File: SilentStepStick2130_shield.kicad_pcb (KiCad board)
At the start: 4 copper layers, 68.6 x 53.3 mm, 15 parts, among them J1 Conn_01x03, U1 TMC2130_SILENTSTEPSTICK, U2 TMC2130_SILENTSTEPSTICK

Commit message: v0
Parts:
- added J2: Conn_01x04_Socket, LibPersoNadj:CUI_TBL009-254-04BK-2OR, F.Cu at (163.2, 87.7)
- added J5: Conn_01x03, Connector_PinHeader_2.54mm:PinHeader_1x03_P2.54mm_Vertical, F.Cu at (128.9, 73.7)
- J1: value Conn_01x03 -> Conn_01x04_Socket; footprint Connector_PinHeader_2.54mm:PinHeader_1x03_P2.54mm_Vertical -> LibPersoNadj:CUI_TBL009-254-04BK-2OR
- moved J1 30.1 mm to (163.2, 61.6), turned to 90 degrees
- moved U1 23.8 mm to (143.5, 64.6)
- moved U2 23.8 mm to (143.5, 86.8)
- moved C1 20.3 mm to (156.2, 95.6), turned to 0 degrees
- moved C2 20.1 mm to (156.2, 73.5), turned to 0 degrees
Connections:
- C1 pad 1: +5V -> /VM
- C2 pad 1: +5V -> /VM
- IOL1 pad 5: /DIR_2 -> /IO4
- IOL1 pad 6: /DIR_1 -> /IO5
- IOL1 pad 7: /IO6 -> /DIR_2
- IOL1 pad 8: /IO7 -> /DIR_1
- J1 pad 1: +5V -> /OA2_1
- J1 pad 2: +5V -> /OA1_1
- J1 pad 3: /VIN -> /OB1_1
- U1 pad 2: /IO3 -> /IO5
- U1 pad 8: /IO7 -> /IO3
- U1 pad 9: +5V -> /VM
- U2 pad 2: /IO2 -> /IO4
- U2 pad 8: /IO6 -> /IO2
- U2 pad 9: +5V -> /VM
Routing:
- net /IO2: track 0.00 -> 72.3 mm
- net /CS_2: track 0.00 -> 55.4 mm
- net /IOREF: track 0.00 -> 55.0 mm
- net /VM: track 0.00 -> 52.1 mm
- net /SCK: track 0.00 -> 50.9 mm
- net /IO4: track 0.00 -> 48.6 mm
- net /MOSI: track 0.00 -> 47.2 mm
- net +5V: track 0.00 -> 45.9 mm
- net /MISO: track 0.00 -> 42.0 mm
- net /IO3: track 0.00 -> 40.5 mm
- net /VIN: track 0.00 -> 40.2 mm
- net /DIR_2: track 0.00 -> 39.3 mm
- net /CS_1: track 0.00 -> 28.5 mm
- net /IO5: track 0.00 -> 25.8 mm
- net /OB1_1: track 0.00 -> 21.2 mm
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
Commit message: v0 sent to fab
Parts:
- moved J5 39.5 mm to (162.6, 94.3), turned to 90 degrees
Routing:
- net +5V: track 45.9 -> 20.4 mm
- net /VIN: track 40.2 -> 17.0 mm
- net /VM: track 52.1 -> 49.0 mm
- net /CS_2: track 55.4 -> 53.3 mm
- net /SCK: track 50.9 -> 51.4 mm
- net GND: vias 368 -> 646

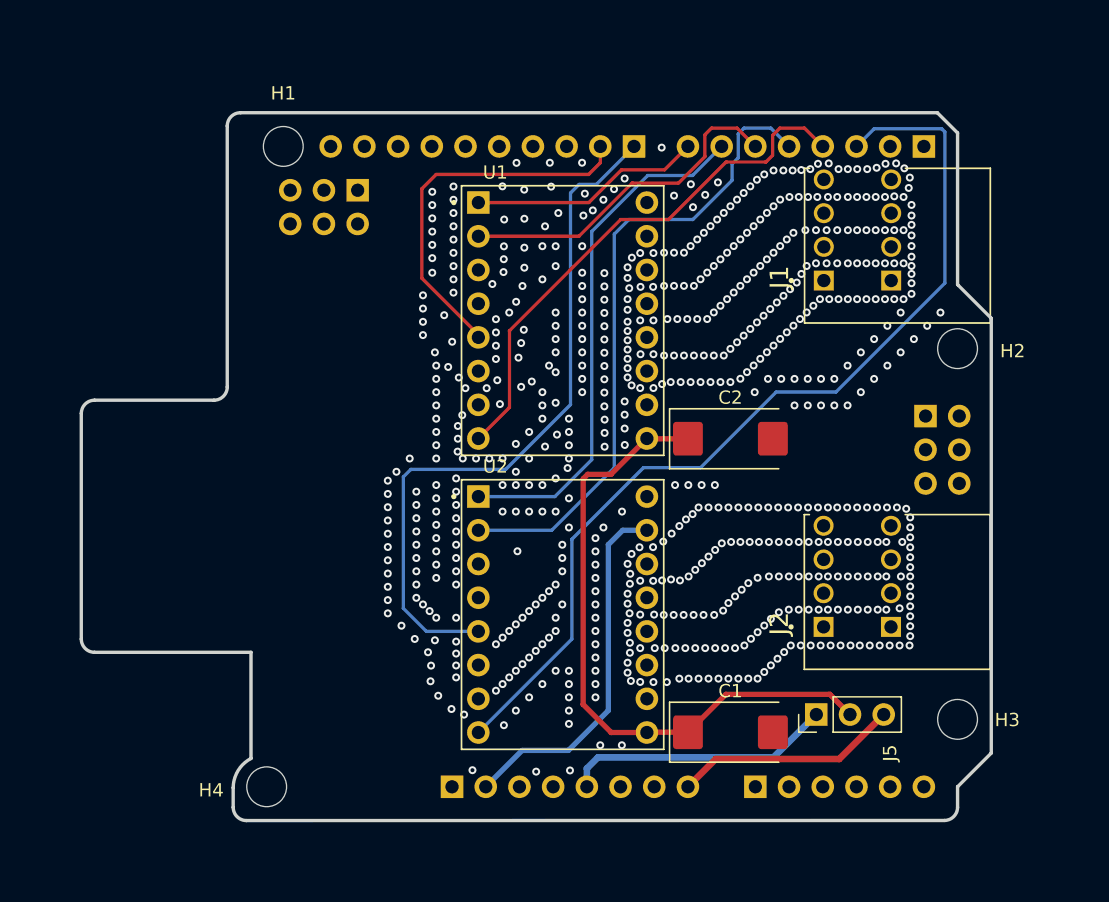
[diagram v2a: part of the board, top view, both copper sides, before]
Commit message: Changed to the new arduino symbol and moved the chipSelect from 11 12 to 12 13 Hard set enables to GND to get 3 digital input free for endcourse contacts Fliped the TMC2130 so that their backside faced up (changed the footprint)
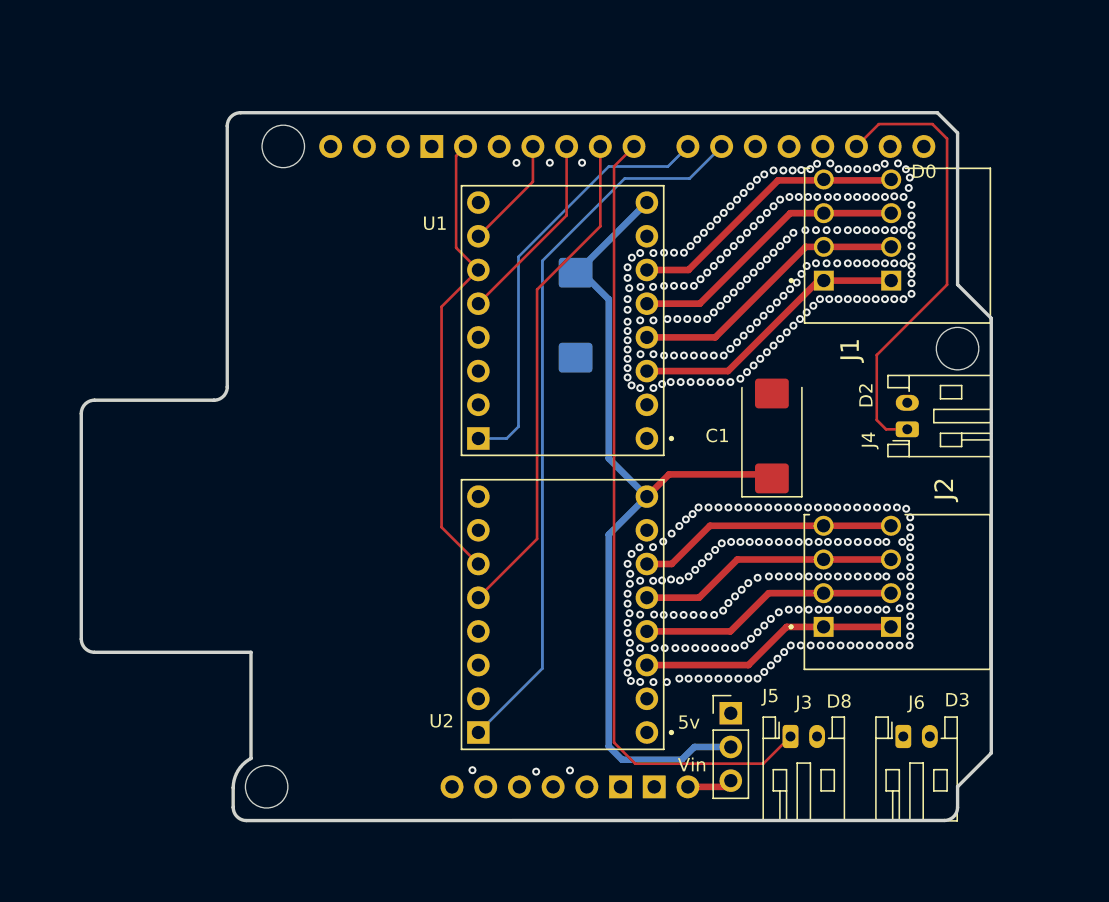
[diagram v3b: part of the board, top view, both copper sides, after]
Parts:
- removed AD1: Conn_01x06_Socket, Connector_PinHeader_2.54mm:PinHeader_1x06_P2.54mm_Vertical
- removed H1, H2, H3, H4: MountingHole, MountingHole:MountingHole_3mm
- removed ICSP1, ICSP2: Conn_02x03_Odd_Even, Connector_PinSocket_2.54mm:PinSocket_2x03_P2.54mm_Vertical
- removed IOH1: Conn_01x10_Socket, Connector_PinHeader_2.54mm:PinHeader_1x10_P2.54mm_Vertical
- removed IOL1, POWER1: Conn_01x08_Socket, Connector_PinHeader_2.54mm:PinHeader_1x08_P2.54mm_Vertical
- added A1: Arduino_Uno_R3_Shield, LibPersoNadj:Arduino_Uno_R3_Shield, F.Cu at (141.5, 75.6)
- added J3: Conn_01x02_Pin, Connector_JST:JST_PH_S2B-PH-K_1x02_P2.00mm_Horizontal, F.Cu at (160.7, 96.0)
- added J4: Conn_01x02_Pin, Connector_JST:JST_PH_S2B-PH-K_1x02_P2.00mm_Horizontal, F.Cu at (169.5, 72.8)
- added J6: Conn_01x02_Pin, Connector_JST:JST_PH_S2B-PH-K_1x02_P2.00mm_Horizontal, F.Cu at (169.2, 96.0)
- C2: moved to B.Cu
- moved C1 22.5 mm to (159.3, 73.3), turned to 90 degrees
- moved C2 14.9 mm to (144.5, 64.2), turned to -90 degrees
- moved J5 6.45 mm to (156.2, 94.2), turned to 0 degrees
- turned U1 to 180 degrees
- turned U2 to 180 degrees
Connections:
- J1 pad 1: /OA2_1 -> /OB2_1
- J1 pad 2: /OA1_1 -> /OB1_1
- J1 pad 3: /OB1_1 -> /OA1_1
- J1 pad 4: /OB2_1 -> /OA2_1
- J2 pad 1: /OA2_2 -> /OB2_2
- J2 pad 2: /OA1_2 -> /OB1_2
- J2 pad 3: /OB1_2 -> /OA1_2
- J2 pad 4: /OB2_2 -> /OA2_2
- U1 pad 2: /IO5 -> /STEP_1
- U1 pad 8: /IO3 -> GND
- U2 pad 2: /IO4 -> /STEP_2
- U2 pad 8: /IO2 -> GND
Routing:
- net Net-(A1-D3_INT1): track 0.00 -> 85.1 mm
- net /IO2: track 72.3 -> 0.00 mm
- net Net-(J3-Pin_1): track 0.00 -> 60.3 mm
- net /STEP_2: track 0.00 -> 57.4 mm
- net /IO4: track 48.6 -> 0.00 mm
- net /IO3: track 40.5 -> 0.00 mm
- net /STEP_1: track 0.00 -> 34.1 mm
- net Net-(A1-D2_INT0): track 0.00 -> 34.0 mm
- net /IO5: track 25.8 -> 0.00 mm
- net +5V: track 20.4 -> 0.00 mm
- net /VM: track 49.0 -> 67.2 mm
- net /SCK: track 51.4 -> 34.7 mm
- net /CS_2: track 53.3 -> 37.8 mm
- net /DIR_2: track 39.3 -> 54.6 mm
- net /MOSI: track 47.2 -> 32.1 mm
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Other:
- board text added: "5v Vin"
- board text added: "D2"
- board text added: "D3"
- board text added: "D8"

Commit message: v1
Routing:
- net Net-(A1-D3_INT1): track 85.1 -> 86.9 mm
- net /DIR_1: track 32.4 -> 33.2 mm
- net /MISO: track 40.0 -> 39.2 mm
- net /STEP_2: track 57.4 -> 56.8 mm
- net Net-(J3-Pin_1): track 60.3 -> 59.7 mm

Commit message: modified shield footprint to reconnect 5v and gnd.kicad_pcb
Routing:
- net +5V: track 0.00 -> 13.9 mm
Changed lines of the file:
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@@
 				(font
 					(size 1.27 1.27)
+					(thickness 0.15)
 				)
 			)
@@
 				(font
 					(size 1.27 1.27)
+					(thickness 0.15)
 				)
 			)
@@
 				(font
 					(size 1.27 1.27)
+					(thickness 0.15)
 				)
 			)
@@
 				(font
 					(size 1.27 1.27)
+					(thickness 0.15)
 				)
 			)
@@
 				(font
 					(size 1.27 1.27)
+					(thickness 0.15)
 				)
 			)
@@
 				(font
 					(size 1.27 1.27)
+					(thickness 0.15)
 				)
 			)
@@
 				(font
 					(size 1.27 1.27)
+					(thickness 0.15)
 				)
 			)
@@
 				(font
 					(size 1.27 1.27)
+					(thickness 0.15)
 				)
 			)
@@
 				(font
 					(size 1.27 1.27)
+					(thickness 0.15)
 				)
 			)
@@
 				(font
 					(size 1.27 1.27)
+					(thickness 0.15)
 				)
 			)
@@
 				(font
 					(size 1.27 1.27)
+					(thickness 0.15)
 				)
 			)
@@
 				(font
 					(size 1.27 1.27)
+					(thickness 0.15)
 				)
 			)
@@
 				(font
 					(size 1.27 1.27)
+					(thickness 0.15)
 				)
 			)
@@
 				(font
 					(size 1.27 1.27)
+					(thickness 0.15)
 				)
 			)
@@
 				(font
 					(size 1.27 1.27)
+					(thickness 0.15)
 				)
 			)
@@
 				(font
 					(size 1.27 1.27)
+					(thickness 0.15)
 				)
 			)
@@
 				(font
 					(size 1.27 1.27)
+					(thickness 0.15)
 				)
 			)
@@
 				(font
 					(size 1.27 1.27)
+					(thickness 0.15)
 				)
 			)
@@
 				(font
 					(size 1.27 1.27)
+					(thickness 0.15)
 				)
 			)
@@
 				(font
 					(size 1.27 1.27)
+					(thickness 0.15)
 				)
 			)
@@
 				(font
 					(size 1.27 1.27)
+					(thickness 0.15)
 				)
 			)
@@
 				(font
 					(size 1.27 1.27)
+					(thickness 0.15)
 				)
 			)
@@
 				(font
 					(size 1.27 1.27)
+					(thickness 0.15)
 				)
 			)
@@
 				(font
 					(size 1.27 1.27)
+					(thickness 0.15)
 				)
 			)
@@
 			(pintype "power_out+no_connect")
 		)
-		(pad "5V" thru_hole oval
+		(pad "5V1" thru_hole oval
 			(at 3.81 24.13)
 			(size 1.7272 1.7272)
@@
 			(layers "*.Cu" "*.Mask")
 			(remove_unused_layers no)
+			(net 8 "+5V")
+			(pinfunction "5V")
+			(pintype "power_in")
 		)
 		(pad "AREF" thru_hole oval
@@
 			(pintype "bidirectional")
 		)
-		(pad "GND" thru_hole rect
-			(at -7.874 -24.13)
+		(pad "GND1" thru_hole rect
+			(at 6.35 24.13)
 			(size 1.7272 1.7272)
 			(drill 1.016)
 			(layers "*.Cu" "*.Mask")
 			(remove_unused_layers no)
+			(net 6 "GND")
+			(pinfunction "GND")
+			(pintype "power_in")
 		)
-		(pad "GND" thru_hole rect
-			(at 6.35 24.13)
+		(pad "GND2" thru_hole rect
+			(at 8.89 24.13)
 			(size 1.7272 1.7272)
 			(drill 1.016)
 			(layers "*.Cu" "*.Mask")
 			(remove_unused_layers no)
+			(net 6 "GND")
+			(pinfunction "GND")
+			(pintype "power_in")
 		)
-		(pad "GND" thru_hole rect
-			(at 8.89 24.13)
+		(pad "GND3" thru_hole rect
+			(at -7.874 -24.13)
 			(size 1.7272 1.7272)
 			(drill 1.016)
 			(layers "*.Cu" "*.Mask")
 			(remove_unused_layers no)
+			(net 6 "GND")
+			(pinfunction "GND")
+			(pintype "power_in")
 		)
 		(pad "IORF" thru_hole oval
@@
 		)
 		(model "${KICAD8_3DMODEL_DIR}/Connector_PinHeader_2.54mm.3dshapes/PinHeader_1x06_P2.54mm_Vertical.step"
-			(hide yes)
 			(offset
 				(xyz 16.5 -24.1 -1.7)
@@
 		)
 		(model "${KICAD8_3DMODEL_DIR}/Connector_PinSocket_2.54mm.3dshapes/PinSocket_2x03_P2.54mm_Vertical.step"
-			(hide yes)
 			(offset
 				(xyz 29.337 3.81 -1.7)
@@
 				(font
 					(size 1.27 1.27)
+					(thickness 0.15)
 				)
 			)
@@
 				(font
 					(size 1.27 1.27)
+					(thickness 0.15)
 				)
 			)
@@
 				(font
 					(size 1.27 1.27)
+					(thickness 0.15)
 				)
 			)
@@
 				(font
 					(size 1.27 1.27)
+					(thickness 0.15)
 				)
 			)
@@
 				(font
 					(size 1.27 1.27)
+					(thickness 0.15)
 				)
 			)
@@
 				(font
 					(size 1.27 1.27)
+					(thickness 0.15)
 				)
 			)
@@
 				(font
 					(size 1.27 1.27)
+					(thickness 0.15)
 				)
 				(justify mirror)
@@
 				(font
 					(size 1.27 1.27)
+					(thickness 0.15)
 				)
 				(justify mirror)
@@
 				(font
 					(size 1.27 1.27)
+					(thickness 0.15)
 				)
 				(justify mirror)
@@
 	)
 	(segment
+		(start 145.35 99.746223)
+		(end 145.35 98.5)
+		(width 0.4)
+		(layer "In2.Cu")
+		(net 8)
+	)
+	(segment
+		(start 151.81 97.54)
+		(end 155.15 94.2)
+		(width 0.4)
+		(layer "In2.Cu")
+		(net 8)
+	)
+	(segment
+		(start 146.31 97.54)
+		(end 151.81 97.54)
+		(width 0.4)
+		(layer "In2.Cu")
+		(net 8)
+	)
+	(segment
+		(start 145.35 98.5)
+		(end 146.31 97.54)
+		(width 0.4)
+		(layer "In2.Cu")
+		(net 8)
+	)
+	(segment
+		(start 155.15 94.2)
+		(end 156.2 94.2)
+		(width 0.4)
+		(layer "In2.Cu")
+		(net 8)
+	)
+	(segment

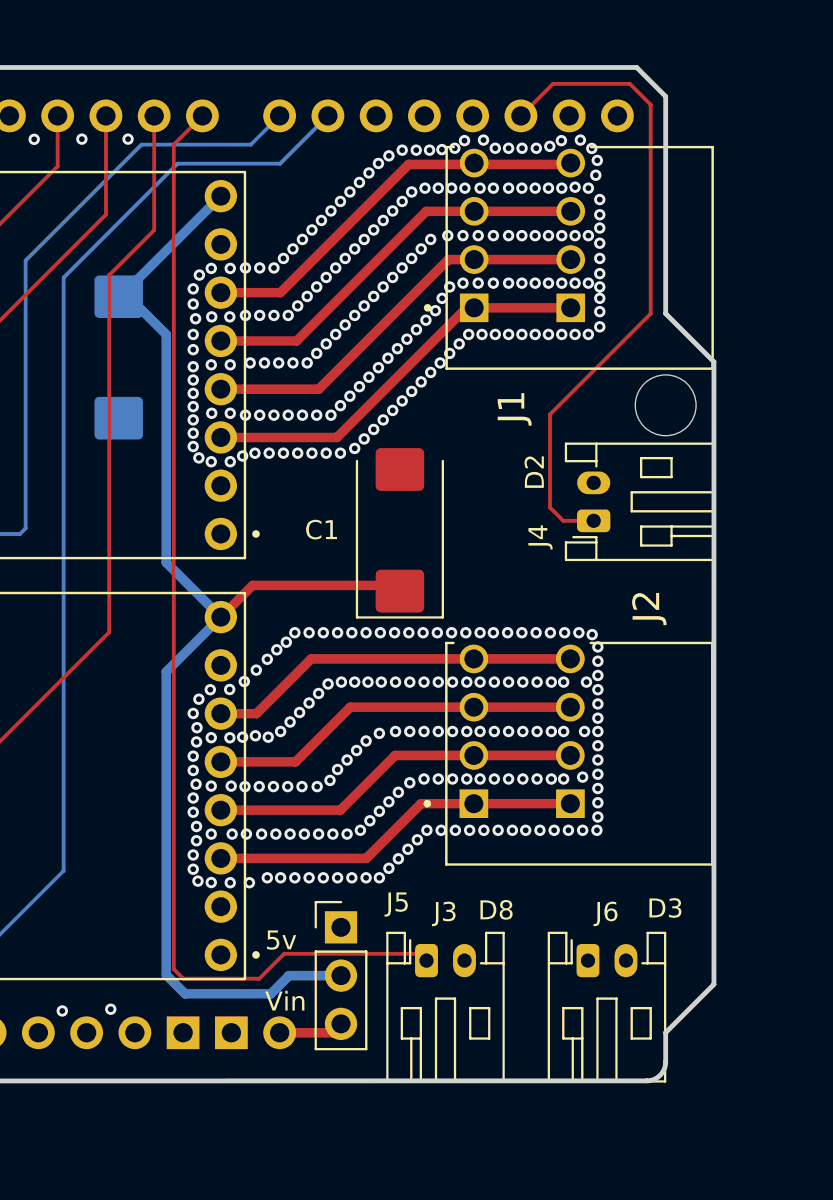
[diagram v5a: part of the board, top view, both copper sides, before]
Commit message: Changed connectors for end course
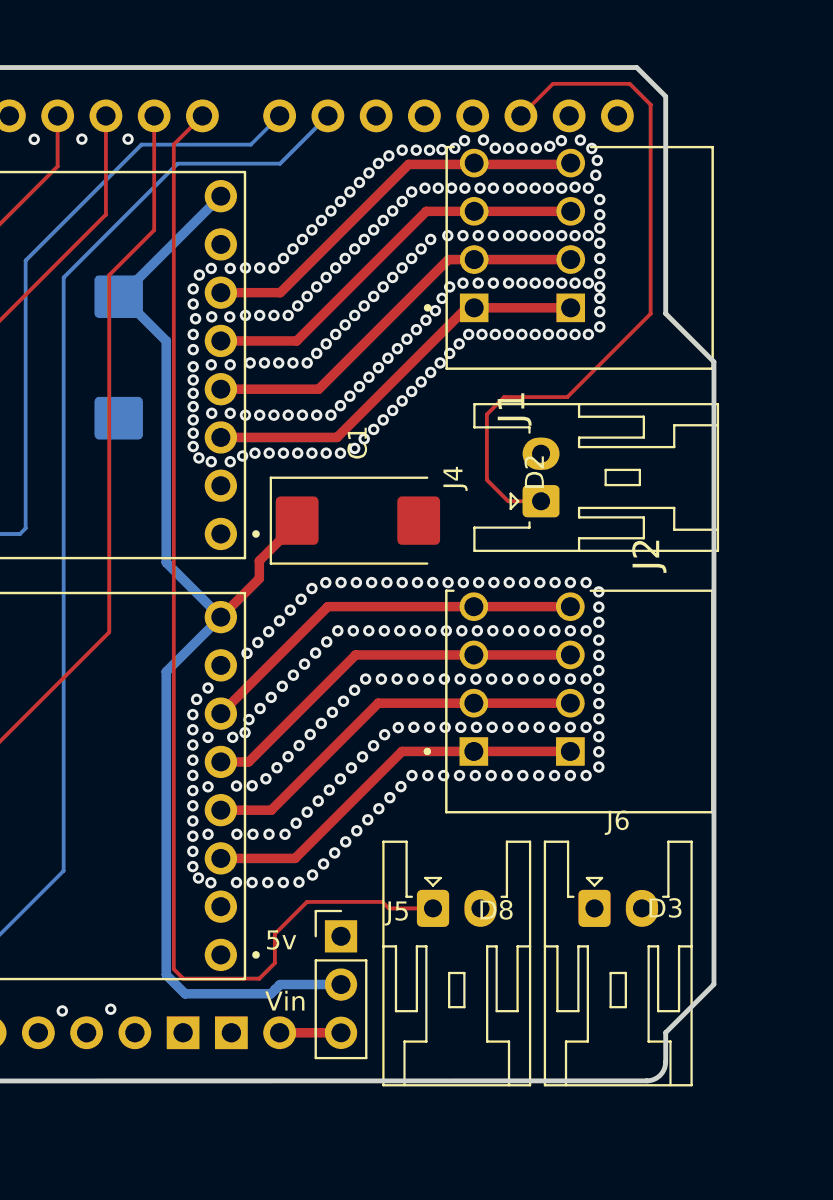
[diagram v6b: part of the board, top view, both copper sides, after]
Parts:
- J3, J4, J6: footprint Connector_JST:JST_PH_S2B-PH-K_1x02_P2.00mm_Horizontal -> Connector_JST:JST_XA_S02B-XASK-1_1x02_P2.50mm_Horizontal
- moved J4 2.96 mm to (166.7, 71.8)
- moved J3 2.77 mm to (161.0, 93.2)
- moved J6 2.77 mm to (169.5, 93.2)
- moved J2 2.75 mm to (163.2, 84.9)
- moved C1 2.27 mm to (157.1, 72.8), turned to 0 degrees
- moved J5 0.47 mm to (156.2, 94.7)
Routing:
- net Net-(A1-D3_INT1): track 86.9 -> 91.8 mm
- net /VM: track 67.2 -> 63.3 mm
- net Net-(A1-D2_INT0): track 34.0 -> 36.6 mm
- net Net-(J3-Pin_1): track 59.7 -> 62.1 mm
- net /OB1_2: track 19.6 -> 20.7 mm
- net /OB2_2: track 19.6 -> 20.7 mm
- net /OA2_2: track 19.6 -> 20.7 mm
- net /OA1_2: track 19.6 -> 20.7 mm
- net GND: vias 361 -> 351

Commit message: v4
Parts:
- added REF**: KiCad-Logo2_6mm_SilkScreen, Symbol:KiCad-Logo2_6mm_SilkScreen, F.Cu at (112.4, 79.9)
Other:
- board text added: "v4"
- board text removed: "D2"
